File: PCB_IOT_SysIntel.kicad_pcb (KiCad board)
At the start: 2 copper layers, 201.8 x 79.6 mm, 72 parts, among them J1 SSW-102-02-G-S, J10 SSW-102-02-G-S, J11 SSW-102-02-G-S, J12 SSW-102-02-G-S, J13 SSW-102-02-G-S, J15 SSW-125-01-T-D-LL, J16 SSW-125-01-T-D-LL, J17 SSW-102-02-G-S, J18 SSW-102-02-G-S, J19 SSW-102-02-G-S, J2 SSW-102-02-G-S, J20 SSW-102-02-G-S, J21 SSW-102-02-G-S, J22 SSW-102-02-G-S, J23 SSW-102-02-G-S, J24 SSW-102-02-G-S, J25 SSW-102-02-G-S, J26 SSW-102-02-G-S, J27 SSW-102-02-G-S, J28 SSW-102-02-G-S, J29 SSW-125-01-T-D-LL, J3 SSW-102-02-G-S, J30 SSW-102-02-G-S, J31 SSW-102-02-G-S, J32 SSW-102-02-G-S, J33 SSW-102-02-G-S, J34 SSW-102-02-G-S, J35 SSW-102-02-G-S, J36 SSW-102-02-G-S, J37 SSW-102-02-G-S, J38 SSW-102-02-G-S, J39 SSW-102-02-G-S, J4 SSW-102-02-G-S, J40 SSW-102-02-G-S, J41 SSW-102-02-G-S, J42 SSW-102-02-G-S, J43 SSW-102-02-G-S, J44 SSW-102-02-G-S, J45 SSW-102-02-G-S, J46 SSW-102-02-G-S, J47 SSW-125-01-T-D-LL, J48 SSW-130-01-T-D-LL, J49 SSW-130-01-T-D-LL, J5 SSW-102-02-G-S, J50 SSW-130-01-T-D-LL, J51 SSW-102-02-G-S, J52 SSW-102-02-G-S, J53 SSW-102-02-G-S, J54 SSW-102-02-G-S, J55 SSW-102-02-G-S, J56 SSW-102-02-G-S, J57 SSW-102-02-G-S, J58 SSW-102-02-G-S, J59 SSW-102-02-G-S, J6 SSW-102-02-G-S, J60 SSW-102-02-G-S, J61 SSW-102-02-G-S, J62 SSW-102-02-G-S, J63 SSW-102-02-G-S, J64 SSW-102-02-G-S, J65 SSW-102-02-G-S, J7 SSW-102-02-G-S, J8 SSW-102-02-G-S, J9 SSW-102-02-G-S, U1 RASPBERRY_PI_4B_4GB

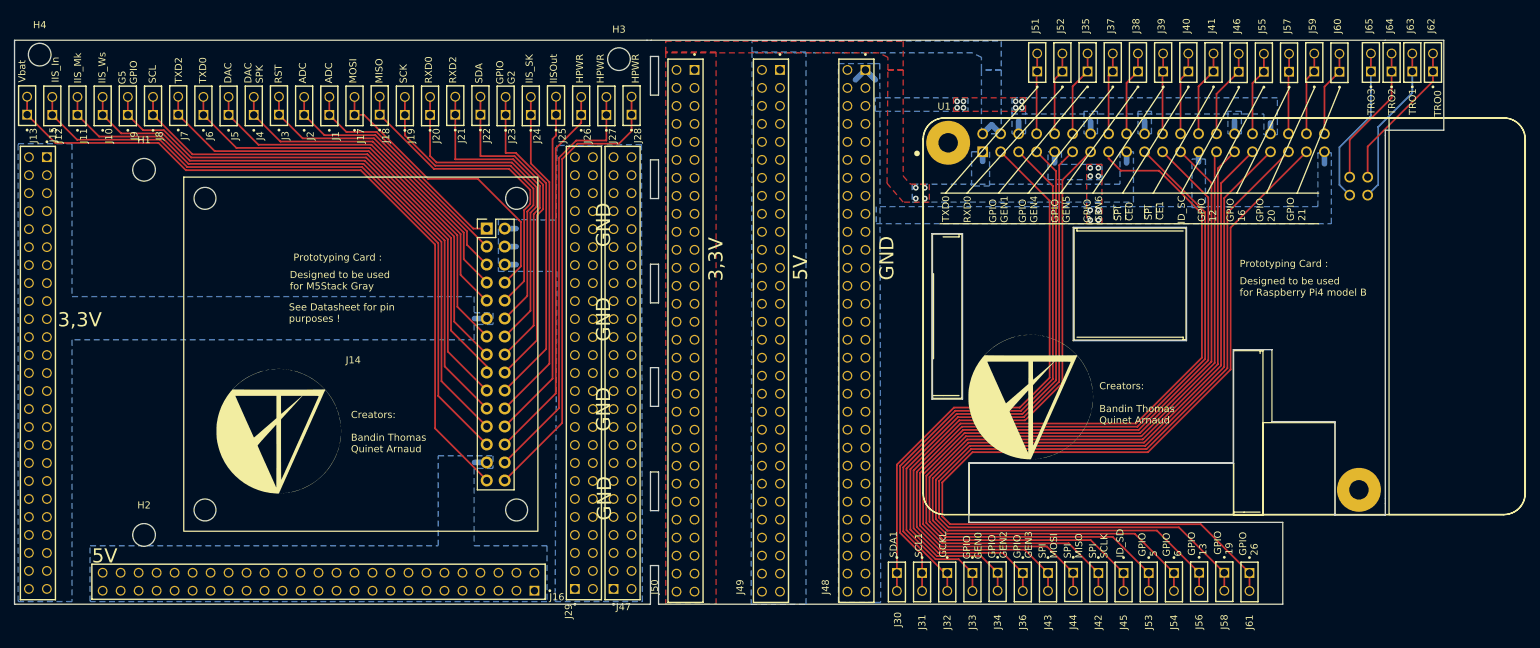
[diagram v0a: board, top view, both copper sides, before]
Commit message: Fixed Mounting hole issues
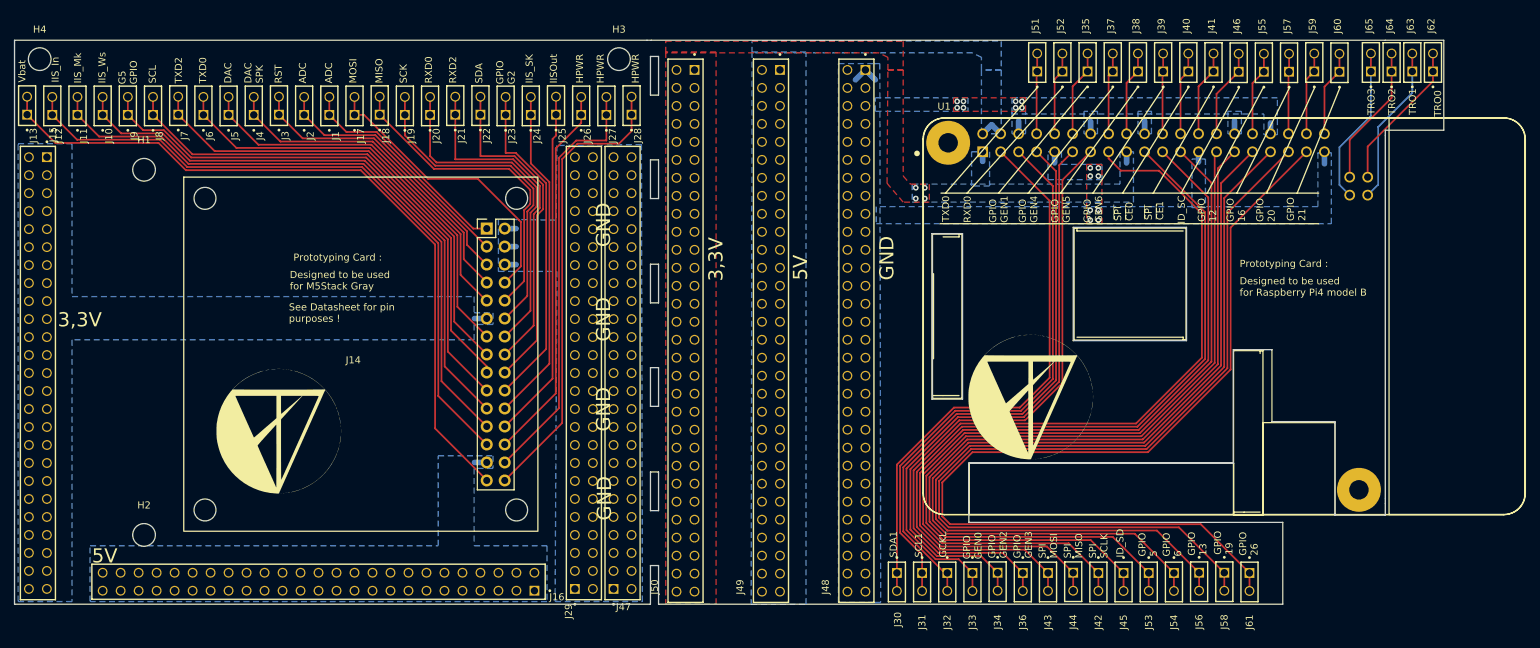
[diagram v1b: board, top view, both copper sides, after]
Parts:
- moved H4 0.64 mm to (23.9, 62.9)
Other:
- board text removed: "Creators: Bandin Thomas Quinet Arnaud"
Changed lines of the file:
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@@
   )
   (footprint "MountingHole:MountingHole_3.2mm_M3" (layer "F.Cu")
-    (at 23.876 62.23)
+    (at 23.876 62.865)
     (descr "Mounting Hole 3.2mm, no annular, M3")
     (tags "mounting hole 3.2mm no annular m3")
@@
         (effects (font (size 1 1) (thickness 0.15)))
     )
-    (fp_text user "${REFERENCE}" (at 0 0) (layer "F.Fab")
+    (fp_text user "${REFERENCE}" (at 0 0.127) (layer "F.Fab")
         (effects (font (size 1 1) (thickness 0.15)))
     )
@@
     (effects (font (size 1 1) (thickness 0.15)) (justify left bottom))
   )
-  (gr_text "Creators: \n\nBandin Thomas\nQuinet Arnaud" (at 67.818 118.491) (layer "F.SilkS")
-    (effects (font (size 1 1) (thickness 0.15)) (justify left bottom))
-  )
   (gr_text "SPI\nCE0" (at 178.308 85.725 90) (layer "F.SilkS")
     (effects (font (size 1 1) (thickness 0.15)) (justify left bottom))
@@
     (effects (font (size 1 1) (thickness 0.15)) (justify left bottom))
   )
-  (gr_text "Creators: \n\nBandin Thomas\nQuinet Arnaud" (at 173.482 114.427) (layer "F.SilkS")
-    (effects (font (size 1 1) (thickness 0.15)) (justify left bottom))
-  )
   (gr_text "GND" (at 104.648 89.408 90) (layer "F.SilkS")
     (effects (font (size 2 2) (thickness 0.15)) (justify left bottom))
@@
         (xy 142.621 139.573)
         (xy 141.732 139.573)
-        (xy 141.732 139.573)
         (xy 136.652 139.573)
